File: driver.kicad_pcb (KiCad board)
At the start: 2 copper layers, 53.8 x 69.1 mm, 26 parts, among them Q1 Q_NMOS_GDSD, Q10 Q_NMOS_GDSD, Q11 Q_NMOS_GDSD, Q12 Q_NMOS_GDSD, Q13 Q_NMOS_GDSD, Q14 Q_NMOS_GDSD, Q15 Q_NMOS_GDSD, Q16 Q_NMOS_GDSD, Q2 Q_NMOS_GDSD, Q3 Q_NMOS_GDSD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

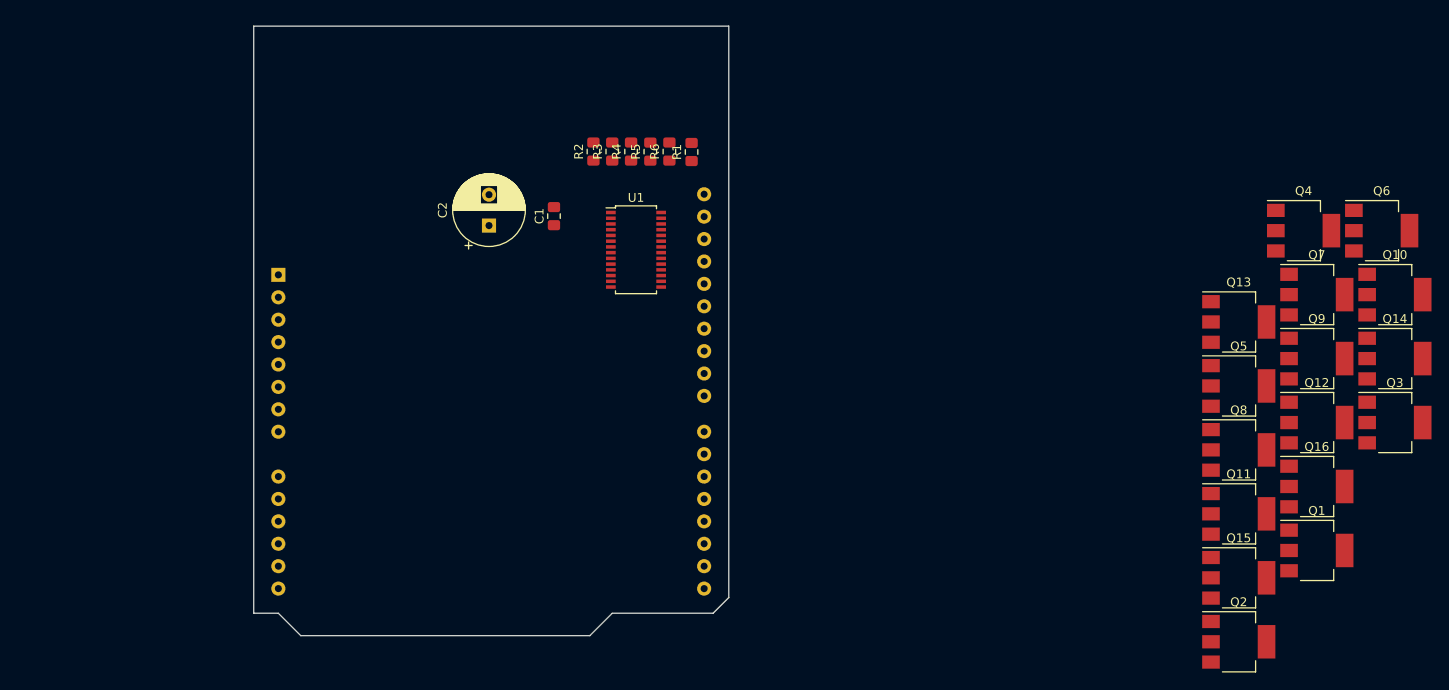
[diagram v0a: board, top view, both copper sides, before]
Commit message: connector selected, beginning routing
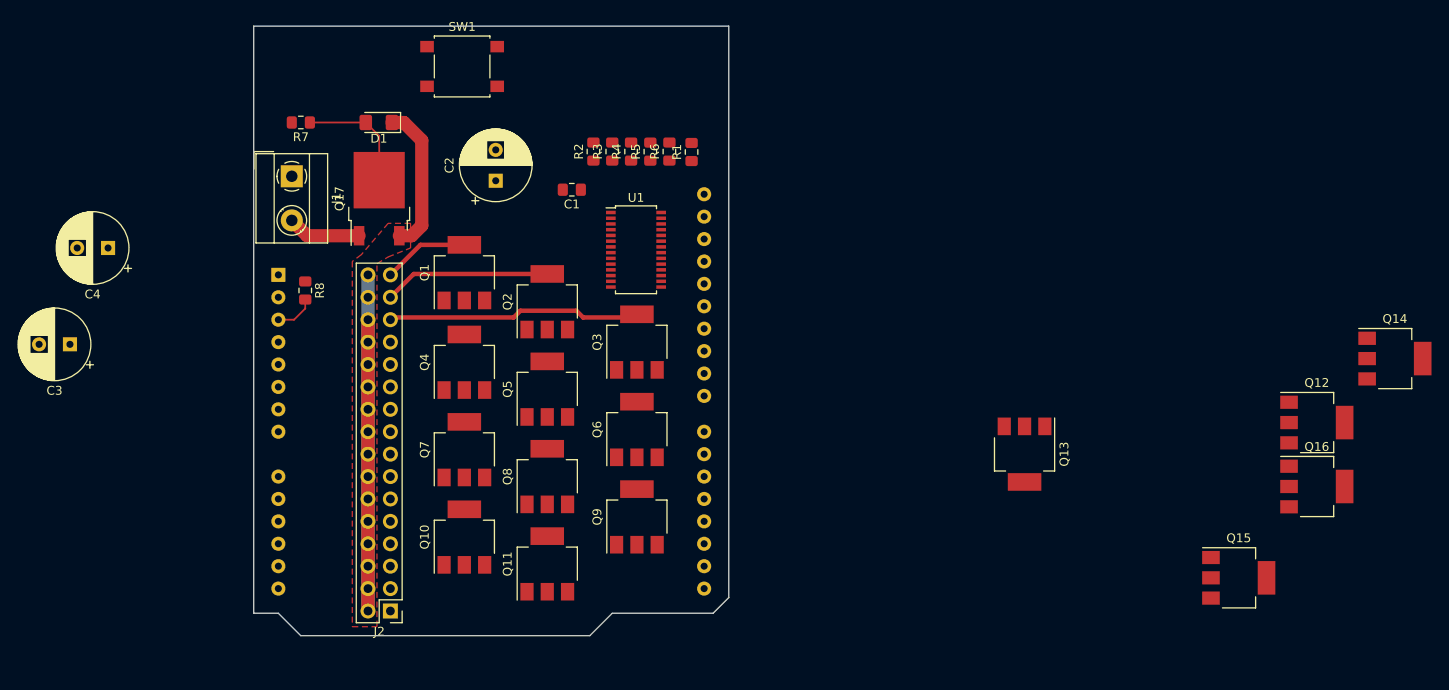
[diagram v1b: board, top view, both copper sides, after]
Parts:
- added C3: 100uF, Capacitor_THT:CP_Radial_D8.0mm_P3.50mm, F.Cu at (54.4, 109.2)
- added C4: 100uF, Capacitor_THT:CP_Radial_D8.0mm_P3.50mm, F.Cu at (58.7, 98.3)
- added D1: Zener 10V, Diode_SMD:D_1206_3216Metric_Pad1.42x1.75mm_HandSolder, F.Cu at (89.4, 84.1)
- added J1: Screw_Terminal_01x02, TerminalBlock_MetzConnect:TerminalBlock_MetzConnect_Type055_RT01502HDWU_1x02_P5.00mm_Horizontal, F.Cu at (79.5, 90.2)
- added J2: Conn_02x16_Odd_Even, Connector_PinHeader_2.54mm:PinHeader_2x16_P2.54mm_Vertical, F.Cu at (90.7, 139.4)
- added Q17: Q_PMOS_DGS, Package_TO_SOT_SMD:TO-252-2, F.Cu at (89.4, 92.7)
- added R7: 100K, Resistor_SMD:R_0805_2012Metric_Pad1.15x1.40mm_HandSolder, F.Cu at (80.5, 84.1)
- added R8: 1K, Resistor_SMD:R_0805_2012Metric_Pad1.15x1.40mm_HandSolder, F.Cu at (81.0, 103.1)
- added SW1: SW_Push, Button_Switch_SMD:SW_SPST_B3S-1000, F.Cu at (98.8, 77.7)
- C2: value 100u -> 100uF
- R1, R2, R3, R4, R5, R6: value 10K -> 1K
- moved Q10 109.0 mm to (99.1, 131.1), turned to 90 degrees
- moved Q1 101.6 mm to (99.1, 101.1), turned to 90 degrees
- moved Q7 98.2 mm to (99.1, 121.2), turned to 90 degrees
- moved Q4 96.3 mm to (99.1, 111.3), turned to 90 degrees
- moved Q6 87.4 mm to (118.6, 118.9), turned to 90 degrees
- moved Q2 87.3 mm to (108.5, 104.4), turned to 90 degrees
- moved Q3 86.4 mm to (118.6, 109.0), turned to 90 degrees
- moved Q9 79.1 mm to (118.6, 128.8), turned to 90 degrees
- moved Q11 78.6 mm to (108.5, 134.1), turned to 90 degrees
- moved Q8 78.4 mm to (108.5, 124.2), turned to 90 degrees
- moved Q5 78.4 mm to (108.5, 114.3), turned to 90 degrees
- moved Q13 28.5 mm to (162.6, 121.7), turned to 270 degrees
- moved C2 5.14 mm to (102.6, 90.7)
- moved C1 3.61 mm to (111.2, 91.7), turned to 180 degrees
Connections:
- A1 pad 29: Net-(A1-Pad29) -> GND
- A1 pad 5: Net-(A1-Pad5) -> VCC
- A1 pad 6: Net-(A1-Pad6) -> GND
- A1 pad 7: Net-(A1-Pad7) -> GND
- Q15 pad 2: Net-(Q15-Pad2) -> PWR_CH2
- Q16 pad 2: Net-(Q16-Pad2) -> PWR_CH3
- Q3 pad 2: Net-(Q3-Pad2) -> PWR_CH13
- U1 pad 13: Net-(U1-Pad13) -> Net-(Q9-Pad1)
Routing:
- net 28V: track 0.00 -> 88.0 mm
- net PWR_CH13: track 0.00 -> 28.8 mm
- net PWR_CH14: track 0.00 -> 18.9 mm
- net Net-(D1-Pad2): track 0.00 -> 13.5 mm
- net PWR_CH15: track 0.00 -> 9.79 mm
- net /input_hicurrent: track 0.00 -> 8.35 mm
- net Net-(A1-Pad3): track 0.00 -> 4.59 mm
- added copper zone on F.Cu, net 28V
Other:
- net class HighCurrent added: clearance 0.254, trace_width 1.5, via_dia 0.8, via_drill 0.4
- net class Power: trace_width 0.381 -> 0.508

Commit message: reroute schematic + component placement
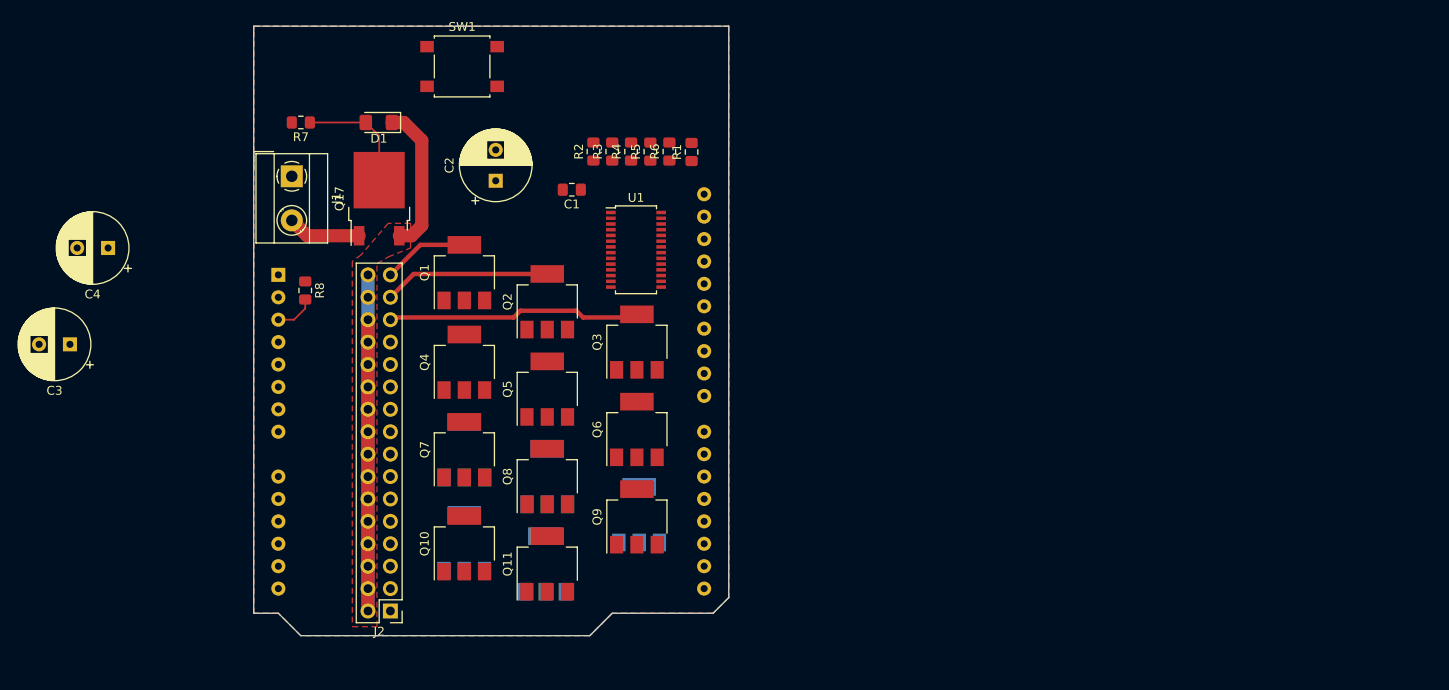
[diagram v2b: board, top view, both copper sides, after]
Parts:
- Q12, Q13, Q14, Q15, Q16: moved to B.Cu
- Q17: value Q_PMOS_DGS -> AOD417 Q_PMOS_DGS
- moved Q14 99.1 mm to (108.2, 134.1), turned to 90 degrees
- moved Q12 96.7 mm to (99.1, 121.2), turned to 90 degrees
- moved Q16 87.2 mm to (108.5, 124.2), turned to 90 degrees
- moved Q15 68.3 mm to (118.9, 128.5), turned to 90 degrees
- moved Q13 64.3 mm to (99.0, 131.7), turned to 90 degrees
- moved Q10 0.76 mm to (99.1, 131.8)
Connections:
- net Net-(Q1-Pad1) renamed /PWM15
- net Net-(Q10-Pad1) renamed /PWM6
- net Net-(Q11-Pad1) renamed /PWM5
- net Net-(Q12-Pad1) renamed /PWM4
- net Net-(Q13-Pad1) renamed /PWM0
- net Net-(Q14-Pad1) renamed /PWM1
- net Net-(Q15-Pad1) renamed /PWM2
- net Net-(Q16-Pad1) renamed /PWM3
- net Net-(Q2-Pad1) renamed /PWM14
- net Net-(Q3-Pad1) renamed /PWM13
- net Net-(Q4-Pad1) renamed /PWM12
- net Net-(Q5-Pad1) renamed /PWM11
- net Net-(Q6-Pad1) renamed /PWM10
- net Net-(Q7-Pad1) renamed /PWM9
- net Net-(Q8-Pad1) renamed /PWM8
- net Net-(Q9-Pad1) renamed /PWM7
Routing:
- added copper zone on B.Cu, net GND
- added copper zone on F.Cu, net GND

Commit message: Trudy's notes
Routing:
- net 28V: track 88.0 -> 99.0 mm
- added copper zone on F.Cu, net (none)
- removed copper zone on F.Cu, net 28V
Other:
- board text added: "separate ground planes?"
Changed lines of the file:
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@@
   (general
     (thickness 1.6)
-    (drawings 9)
-    (tracks 36)
+    (drawings 10)
+    (tracks 40)
     (zones 0)
     (modules 35)
@@
     (47 F.CrtYd user)
     (48 B.Fab user)
-    (49 F.Fab user hide)
+    (49 F.Fab user)
   )
   (setup
@@
     (mod_text_size 1 1)
     (mod_text_width 0.15)
-    (pad_size 2 1.5)
-    (pad_drill 0)
+    (pad_size 2.5 2.5)
+    (pad_drill 1.3)
     (pad_to_mask_clearance 0.051)
     (solder_mask_min_width 0.25)
     (aux_axis_origin 0 0)
-    (visible_elements FFFFFF7F)
+    (visible_elements FFFFF77F)
     (pcbplotparams
       (layerselection 0x010fc_ffffffff)
@@
     )
     (pad 1 thru_hole rect (at 0 0 270) (size 2.5 2.5) (drill 1.3) (layers *.Cu *.Mask)
-      (net 29 GND))
+      (net 29 GND) (zone_connect 2))
     (pad 2 thru_hole circle (at 5 0 270) (size 2.5 2.5) (drill 1.3) (layers *.Cu *.Mask)
       (net 57 /input_hicurrent))
@@
     )
   )
+  (gr_text "separate ground planes?" (at 147.574 85.344) (layer F.Fab)
+    (effects (font (size 1.5 1.5) (thickness 0.3)))
+  )
   (gr_line (start 75.184 139.7) (end 75.184 73.152) (layer Edge.Cuts) (width 0.15))
   (gr_line (start 77.978 139.7) (end 75.184 139.7) (layer Edge.Cuts) (width 0.15))
@@
   (segment (start 88.138 119.126) (end 88.138 116.586) (width 1.5) (layer B.Cu) (net 54))
   (segment (start 88.138 116.586) (end 88.138 101.346) (width 1.5) (layer B.Cu) (net 54))
+  (segment (start 88.138 101.346) (end 88.138 106.426) (width 1.5) (layer F.Cu) (net 54))
+  (segment (start 88.138 101.346) (end 88.138 100.46) (width 1.5) (layer F.Cu) (net 54))
+  (segment (start 88.138 100.46) (end 90.046 98.552) (width 1.5) (layer F.Cu) (net 54))
+  (segment (start 90.046 98.552) (end 91.688 96.91) (width 1.5) (layer F.Cu) (net 54))
   (segment (start 89.408 85.598) (end 87.884 84.074) (width 0.2032) (layer F.Cu) (net 56))
   (segment (start 89.408 90.61) (end 89.408 85.598) (width 0.2032) (layer F.Cu) (net 56))
@@
   (segment (start 81.242 96.91) (end 79.502 95.17) (width 1.5) (layer F.Cu) (net 57))
   (segment (start 87.128 96.91) (end 81.242 96.91) (width 1.5) (layer F.Cu) (net 57))
-  (zone (net 54) (net_name 28V) (layer F.Cu) (hatch edge 0.508)
+  (zone (net 0) (net_name "") (layer F.Cu) (hatch edge 0.508)
     (connect_pads (clearance 0.508))
     (min_thickness 0.254)
-    (fill (arc_segments 16) (thermal_gap 0.508) (thermal_bridge_width 0.508))
+    (fill yes (arc_segments 16) (thermal_gap 0.508) (thermal_bridge_width 0.508))
     (polygon
       (pts
@@
     (connect_pads (clearance 0.508))
     (min_thickness 0.254)
-    (fill (arc_segments 16) (thermal_gap 0.508) (thermal_bridge_width 0.508))
+    (fill yes (arc_segments 16) (thermal_gap 0.508) (thermal_bridge_width 0.508))
     (polygon
       (pts
@@
     (connect_pads (clearance 0.508))
     (min_thickness 0.254)
-    (fill (arc_segments 16) (thermal_gap 0.508) (thermal_bridge_width 0.508))
+    (fill yes (arc_segments 16) (thermal_gap 0.508) (thermal_bridge_width 0.508))
     (polygon
       (pts

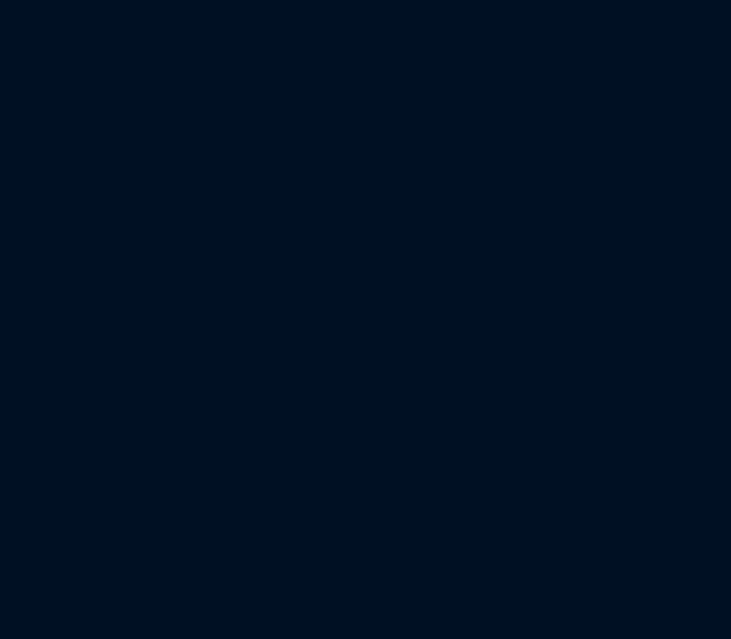
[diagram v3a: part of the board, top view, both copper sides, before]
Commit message: add pulldown resistors
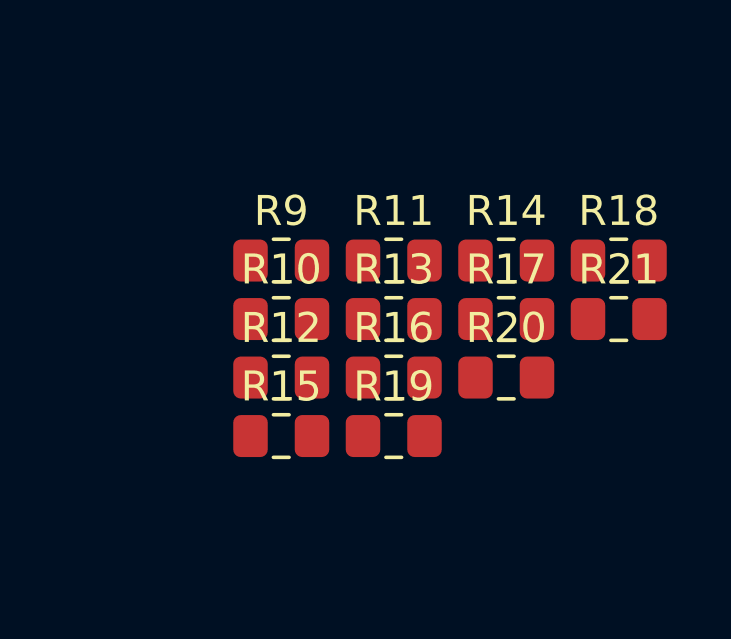
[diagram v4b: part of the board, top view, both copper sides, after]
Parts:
- added R10: 10k, Resistor_SMD:R_0805_2012Metric_Pad1.15x1.40mm_HandSolder, F.Cu at (148.7, 113.2)
- added R11: 10k, Resistor_SMD:R_0805_2012Metric_Pad1.15x1.40mm_HandSolder, F.Cu at (152.4, 111.2)
- added R12: 10k, Resistor_SMD:R_0805_2012Metric_Pad1.15x1.40mm_HandSolder, F.Cu at (148.7, 115.1)
- added R13: 10k, Resistor_SMD:R_0805_2012Metric_Pad1.15x1.40mm_HandSolder, F.Cu at (152.4, 113.2)
- added R14: 10k, Resistor_SMD:R_0805_2012Metric_Pad1.15x1.40mm_HandSolder, F.Cu at (156.2, 111.2)
- added R15: 10k, Resistor_SMD:R_0805_2012Metric_Pad1.15x1.40mm_HandSolder, F.Cu at (148.7, 117.1)
- added R16: 10k, Resistor_SMD:R_0805_2012Metric_Pad1.15x1.40mm_HandSolder, F.Cu at (152.4, 115.1)
- added R17: 10k, Resistor_SMD:R_0805_2012Metric_Pad1.15x1.40mm_HandSolder, F.Cu at (156.2, 113.2)
- added R18: 10k, Resistor_SMD:R_0805_2012Metric_Pad1.15x1.40mm_HandSolder, F.Cu at (159.9, 111.2)
- added R19: 10k, Resistor_SMD:R_0805_2012Metric_Pad1.15x1.40mm_HandSolder, F.Cu at (152.4, 117.1)
- added R20: 10k, Resistor_SMD:R_0805_2012Metric_Pad1.15x1.40mm_HandSolder, F.Cu at (156.2, 115.1)
- added R21: 10k, Resistor_SMD:R_0805_2012Metric_Pad1.15x1.40mm_HandSolder, F.Cu at (159.9, 113.2)
- added R9: 10k, Resistor_SMD:R_0805_2012Metric_Pad1.15x1.40mm_HandSolder, F.Cu at (148.7, 111.2)
- C3: value 100uF -> CP
- C4: value 100uF -> C
- R2, R3, R4, R5, R6: value 1K -> 10k
- R7: value 100K -> 10K
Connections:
- C3 pad 2: Net-(C3-Pad2) -> GND
- C4 pad 1: Net-(C3-Pad2) -> 28V
- R2 pad 1: Net-(R2-Pad1) -> VCC
- R2 pad 2: VCC -> /SDA
- R3 pad 1: Net-(R3-Pad1) -> VCC
- R3 pad 2: VCC -> /SCL
- R4 pad 1: Net-(R4-Pad1) -> /PWM0
- R4 pad 2: VCC -> GND
- R5 pad 1: Net-(R5-Pad1) -> /PWM1
- R5 pad 2: VCC -> GND
- R6 pad 1: Net-(R6-Pad1) -> /PWM2
- R6 pad 2: VCC -> GND
- U1 pad 1: Net-(R6-Pad1) -> Net-(R1-Pad1)
- U1 pad 2: Net-(R5-Pad1) -> Net-(R1-Pad1)
- U1 pad 3: Net-(R4-Pad1) -> Net-(R1-Pad1)
- U1 pad 4: Net-(R3-Pad1) -> Net-(R1-Pad1)
- U1 pad 5: Net-(R2-Pad1) -> Net-(R1-Pad1)

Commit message: change address
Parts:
- added R22: 1K, Resistor_SMD:R_0805_2012Metric_Pad1.15x1.40mm_HandSolder, F.Cu at (112.8, 87.9)
- added R23: 1K, Resistor_SMD:R_0805_2012Metric_Pad1.15x1.40mm_HandSolder, F.Cu at (120.9, 87.9)
- added R24: 1K, Resistor_SMD:R_0805_2012Metric_Pad1.15x1.40mm_HandSolder, F.Cu at (118.9, 87.9)
- added R25: 1K, Resistor_SMD:R_0805_2012Metric_Pad1.15x1.40mm_HandSolder, F.Cu at (114.8, 87.9)
- added R26: 1K, Resistor_SMD:R_0805_2012Metric_Pad1.15x1.40mm_HandSolder, F.Cu at (116.8, 87.9)
- moved R4 35.5 mm to (144.3, 111.3), turned to 0 degrees
- moved R5 35.3 mm to (149.3, 107.2), turned to 0 degrees
- moved R6 29.9 mm to (144.3, 107.7), turned to 180 degrees
- moved R1 14.1 mm to (110.7, 87.9)
- moved R2 10.8 mm to (124.5, 87.4), turned to 270 degrees
- moved R3 10.7 mm to (126.5, 87.4), turned to 270 degrees
- moved C1 5.33 mm to (111.2, 97.0)
- moved U1 4.03 mm to (118.9, 94.5), turned to 270 degrees
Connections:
- R1 pad 2: VCC -> GND
- U1 pad 1: Net-(R1-Pad1) -> Net-(R26-Pad1)
- U1 pad 2: Net-(R1-Pad1) -> Net-(R25-Pad1)
- U1 pad 25: Net-(U1-Pad25) -> GND
- U1 pad 3: Net-(R1-Pad1) -> Net-(R24-Pad1)
- U1 pad 4: Net-(R1-Pad1) -> Net-(R23-Pad1)
- U1 pad 5: Net-(R1-Pad1) -> Net-(R22-Pad1)
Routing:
- net PWR_CH13: track 28.8 -> 0.00 mm
- net PWR_CH14: track 18.9 -> 0.00 mm
- net PWR_CH15: track 9.79 -> 0.00 mm
